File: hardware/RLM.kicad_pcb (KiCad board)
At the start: 2 copper layers, 3 parts, among them U1 ESP32, U2 NRF24L01+, U3 MPU-6050

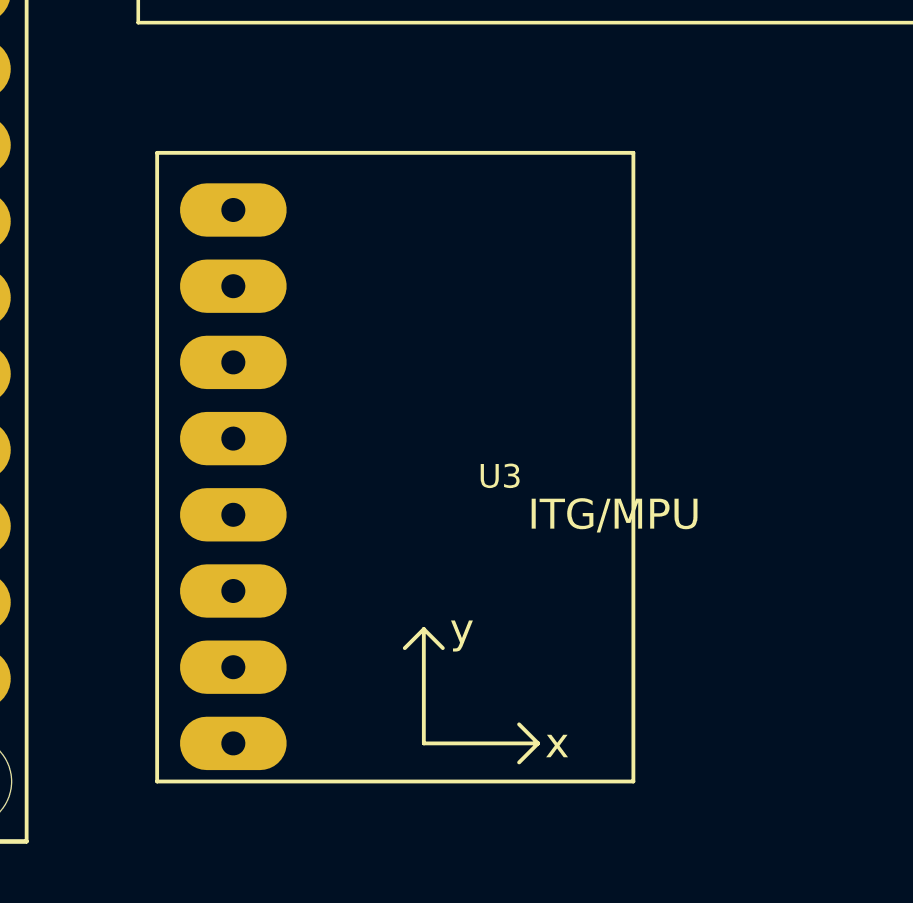
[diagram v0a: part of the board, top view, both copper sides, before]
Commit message: feat: add custom ESP32, NRF, GY modules
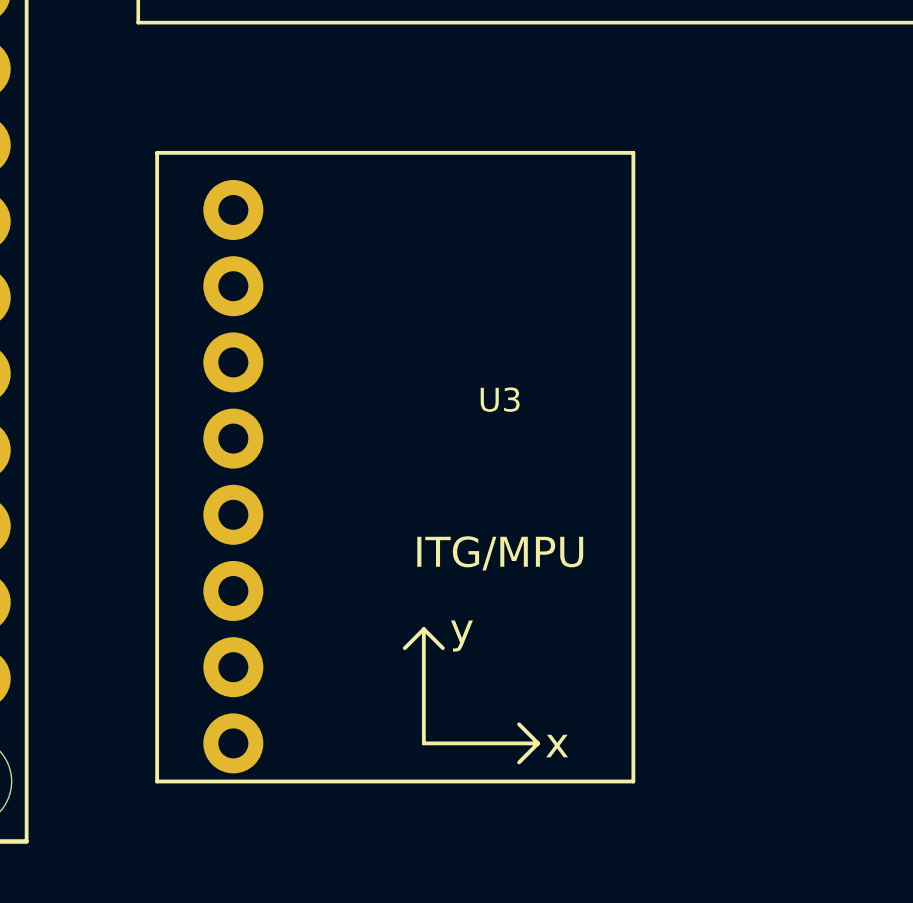
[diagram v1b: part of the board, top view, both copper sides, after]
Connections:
- net 3V3 renamed +3.3V
